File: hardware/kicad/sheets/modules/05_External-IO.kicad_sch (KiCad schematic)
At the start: 0 parts

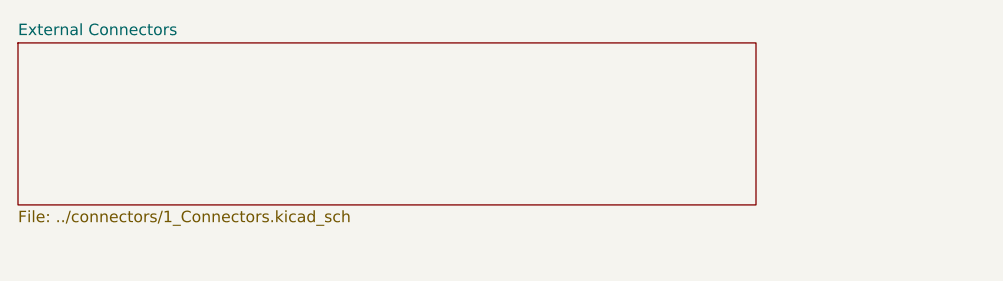
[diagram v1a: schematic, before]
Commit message: netties and better sheet nesting for servo connectors
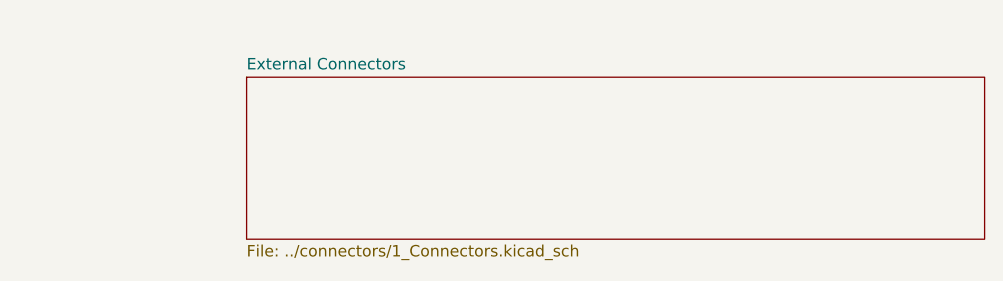
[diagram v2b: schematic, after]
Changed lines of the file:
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@@
 	)
 	(sheet
-		(at 10 15)
+		(at 35.4 18.81)
 		(size 82 18)
 		(exclude_from_sim no)
@@
 		)
 		(property "Sheetname" "External Connectors"
-			(at 10 14.2884 0)
+			(at 35.4 18.0984 0)
 			(effects
 				(font
@@
 		)
 		(property "Sheetfile" "../connectors/1_Connectors.kicad_sch"
-			(at 10 33.5846 0)
+			(at 35.4 37.3946 0)
 			(effects
 				(font

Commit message: current sensing on the servos and cleaning up empty sheets
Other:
- removed sheet External Connectors
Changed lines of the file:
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@@
 		(date "2026-02-16")
 	)
-	(sheet
-		(at 35.4 18.81)
-		(size 82 18)
-		(exclude_from_sim no)
-		(in_bom yes)
-		(on_board yes)
-		(dnp no)
-		(fields_autoplaced yes)
-		(stroke
-			(width 0)
-			(type solid)
-		)
-		(fill
-			(color 0 0 0 0.0000)
-		)
-		(property "Sheetname" "External Connectors"
-			(at 35.4 18.0984 0)
-			(effects
-				(font
-					(size 1.27 1.27)
-				)
-				(justify left bottom)
-			)
-		)
-		(property "Sheetfile" "../connectors/1_Connectors.kicad_sch"
-			(at 35.4 37.3946 0)
-			(effects
-				(font
-					(size 1.27 1.27)
-				)
-				(justify left top)
-			)
-		)
-	)
 )
